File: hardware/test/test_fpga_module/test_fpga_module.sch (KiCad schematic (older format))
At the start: 2 parts, among them J1 Conn_02x26_Odd_Even, J2 Conn_02x26_Odd_Even

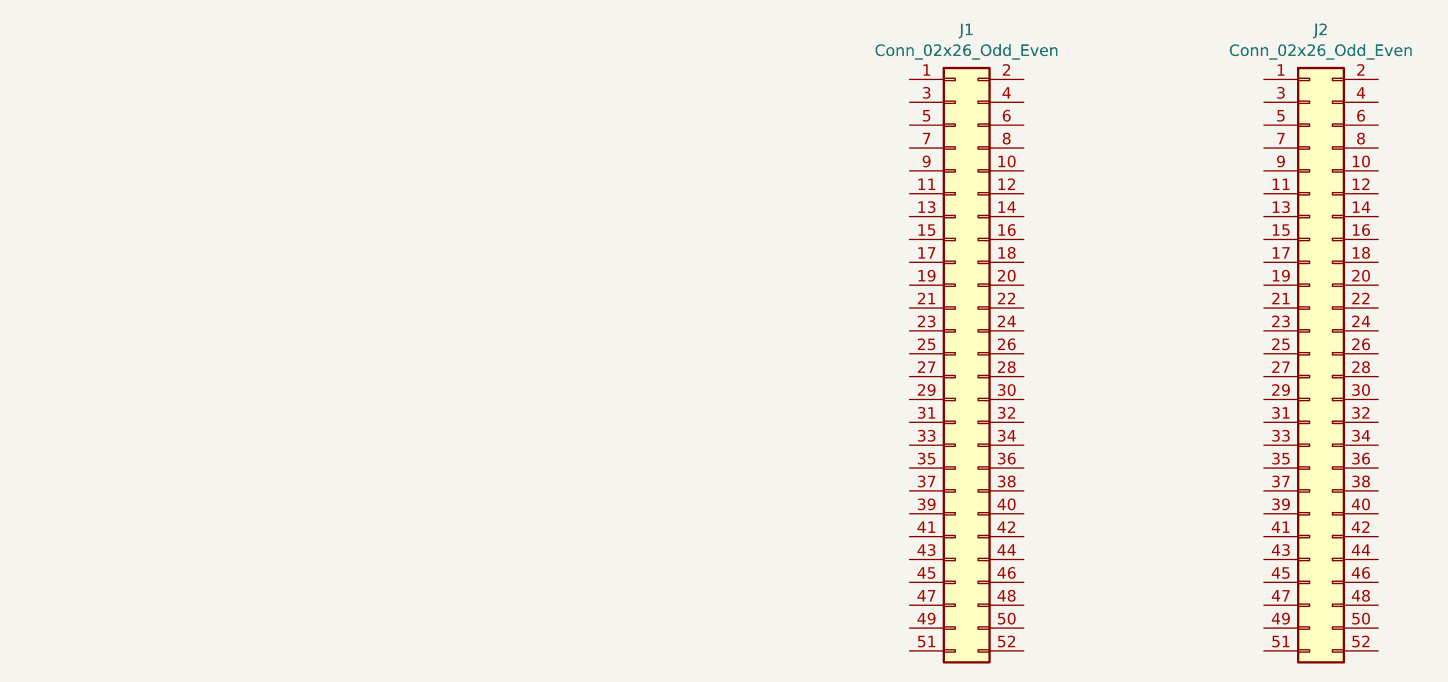
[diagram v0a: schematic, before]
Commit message: busses added
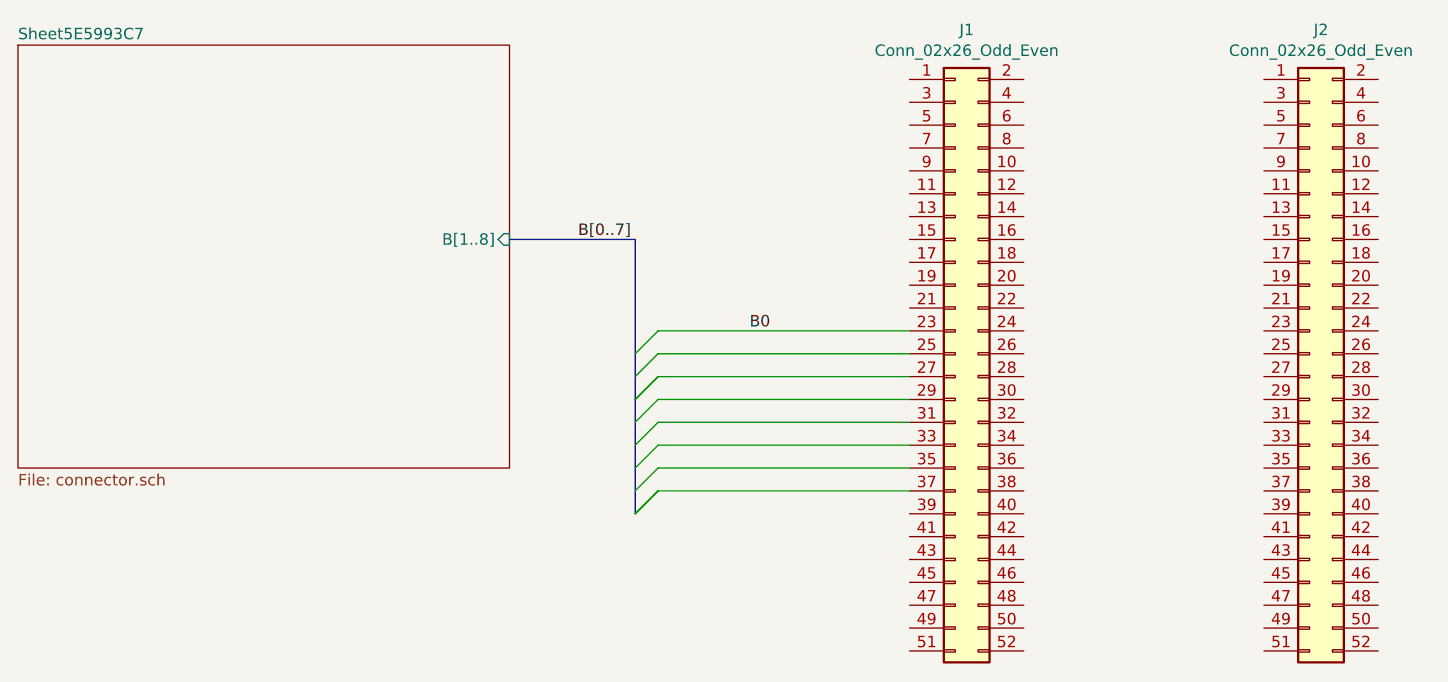
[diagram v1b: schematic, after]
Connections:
- net B0: now reaches J1.23 (Pin_23)
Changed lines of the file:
@@
 $Descr A4 11693 8268
 encoding utf-8
-Sheet 1 1
+Sheet 1 2
 Title ""
 Date ""
@@
 	1    0    0    -1
 $EndComp
+$Sheet
+S 1500 1750 2150 1850
+U 5E5993C8
+F0 "Sheet5E5993C7" 50
+F1 "connector.sch" 50
+F2 "B[1..8]" I R 3650 2600 50
+$EndSheet
+Wire Bus Line
+	3650 2600 4200 2600
+Entry Wire Line
+	4200 3800 4300 3700
+Entry Wire Line
+	4200 3800 4300 3700
+Entry Wire Line
+	4200 3700 4300 3600
+Entry Wire Line
+	4200 3600 4300 3500
+Entry Wire Line
+	4200 3500 4300 3400
+Entry Wire Line
+	4200 3400 4300 3300
+Entry Wire Line
+	4200 3300 4300 3200
+Entry Wire Line
+	4200 3300 4300 3200
+Entry Wire Line
+	4200 3200 4300 3100
+Entry Wire Line
+	4200 3100 4300 3000
+Wire Wire Line
+	4300 3000 5400 3000
+Wire Wire Line
+	5400 3100 4300 3100
+Wire Wire Line
+	4300 3200 5400 3200
+Wire Wire Line
+	5400 3300 4300 3300
+Wire Wire Line
+	4300 3400 5400 3400
+Wire Wire Line
+	5400 3500 4300 3500
+Wire Wire Line
+	4300 3600 5400 3600
+Wire Wire Line
+	5400 3700 4300 3700
+Wire Bus Line
+	4200 2600 4200 3800
+Text Label 3950 2600 0    50   ~ 0
+B[0..7]
+Text Label 4700 3000 0    50   ~ 0
+B0
 $EndSCHEMATC
